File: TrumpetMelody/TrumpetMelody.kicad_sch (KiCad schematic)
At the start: 75 parts, among them J1 USB_B_Micro, J2 Conn_01x05, SW1 SW_Push, SW2 SW_SPST, SW3 SW_SPST, SW4 SW_SPST, U1 STM32F411RETx, U2 TLV62565DBVR, U3 MAX98357AETE+T, Y1 8MHz

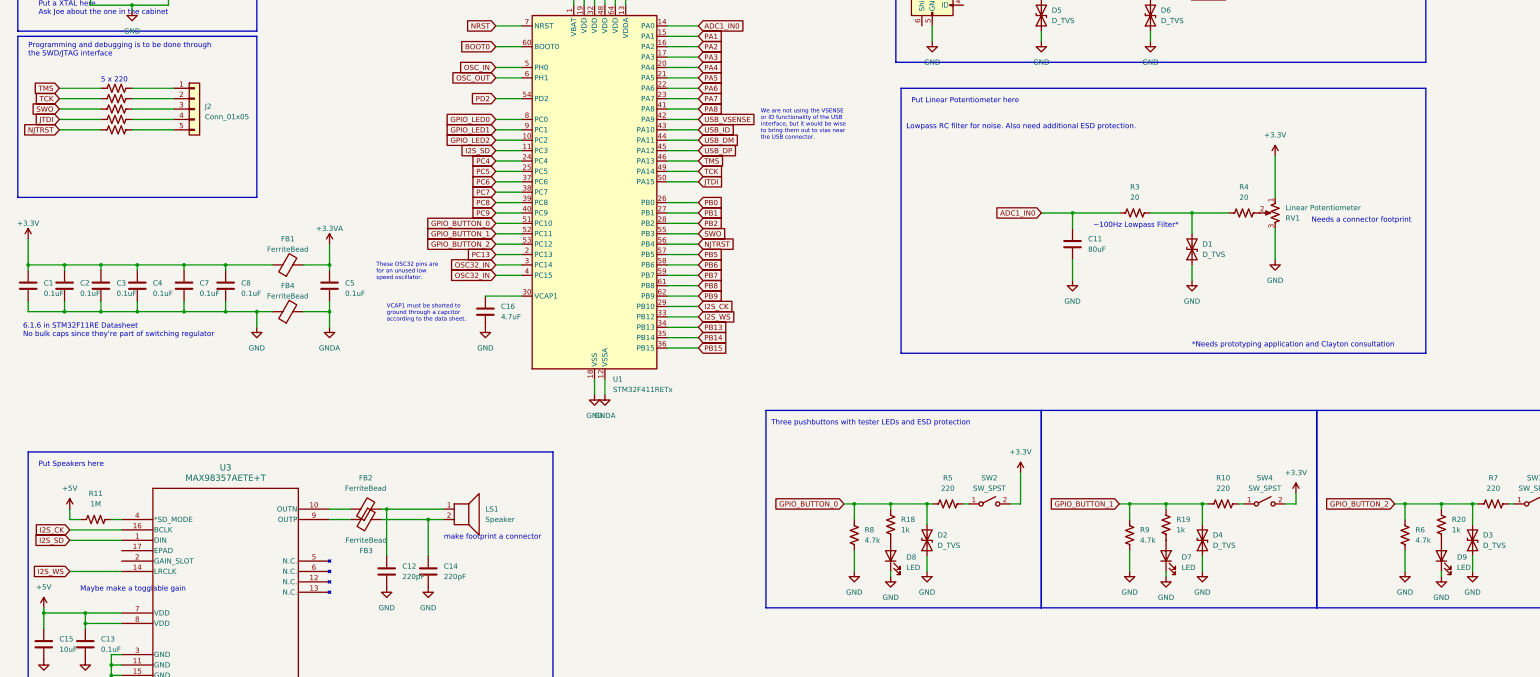
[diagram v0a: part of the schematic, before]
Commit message: Added gain resistor to speaker circuit
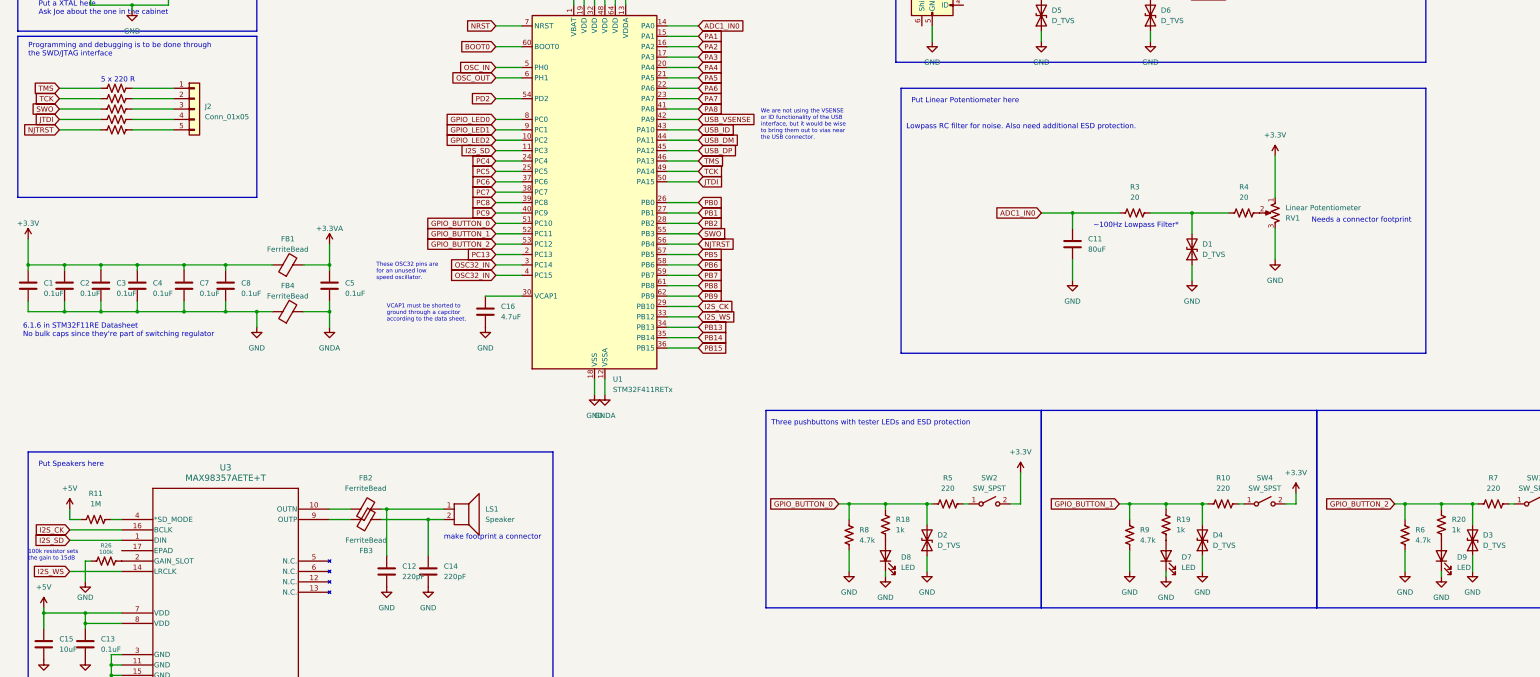
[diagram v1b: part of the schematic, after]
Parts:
- added R26: 100k, Resistor_SMD:R_0805_2012Metric_Pad1.20x1.40mm_HandSolder, symbol Device:R_US
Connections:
- net GND: now also R26.1
- net at U3.2 (GAIN_SLOT): now also R26.2
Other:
- note added: "100k resistor sets the gain to 15dB"
- note added: "5 x 220 R"
- note removed: "*Needs prototyping application and Clayton consultation"
- note removed: "5 x 220"
- note removed: "Maybe make a togglable gain"
- moved on the sheet: D8, R18, R8
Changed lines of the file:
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@@
   (junction (at 26.67 175.26) (diameter 0) (color 0 0 0 0)
   )
-  (junction (at 228.6 222.25) (diameter 0) (color 0 0 0 0)
+  (junction (at 227.33 222.25) (diameter 0) (color 0 0 0 0)
   )
   (junction (at 370.84 222.25) (diameter 0) (color 0 0 0 0)
@@
   (junction (at 31.75 248.92) (diameter 0) (color 0 0 0 0)
   )
-  (junction (at 219.71 222.25) (diameter 0) (color 0 0 0 0)
+  (junction (at 218.44 222.25) (diameter 0) (color 0 0 0 0)
   )
   (junction (at 354.33 222.25) (diameter 0) (color 0 0 0 0)
@@
     (stroke (width 0) (type default))
   )
-  (wire (pts (xy 228.6 222.25) (xy 228.6 223.52))
+  (wire (pts (xy 227.33 222.25) (xy 227.33 223.52))
     (stroke (width 0) (type default))
   )
@@
     (stroke (width 0) (type default))
   )
-  (wire (pts (xy 219.71 222.25) (xy 228.6 222.25))
+  (wire (pts (xy 218.44 222.25) (xy 227.33 222.25))
     (stroke (width 0) (type default))
   )
@@
     (stroke (width 0) (type default))
   )
-  (wire (pts (xy 228.6 238.76) (xy 228.6 240.03))
+  (wire (pts (xy 227.33 238.76) (xy 227.33 240.03))
     (stroke (width 0) (type default))
   )
@@
     (stroke (width 0) (type default))
   )
+  (wire (pts (xy 31.75 236.22) (xy 31.75 241.3))
+    (stroke (width 0) (type default))
+  )
   (wire (pts (xy 273.05 154.94) (xy 273.05 151.13))
     (stroke (width 0) (type default))
@@
     (stroke (width 0) (type default))
   )
+  (wire (pts (xy 33.02 236.22) (xy 31.75 236.22))
+    (stroke (width 0) (type default))
+  )
   (wire (pts (xy 17.78 157.48) (xy 17.78 163.83))
     (stroke (width 0) (type default))
@@
     (stroke (width 0) (type default))
   )
-  (wire (pts (xy 217.17 222.25) (xy 219.71 222.25))
+  (wire (pts (xy 215.9 222.25) (xy 218.44 222.25))
     (stroke (width 0) (type default))
   )
@@
     (stroke (width 0) (type default))
   )
-  (wire (pts (xy 219.71 233.68) (xy 219.71 238.76))
+  (wire (pts (xy 218.44 233.68) (xy 218.44 238.76))
     (stroke (width 0) (type default))
   )
@@
     (stroke (width 0) (type default))
   )
-  (wire (pts (xy 219.71 222.25) (xy 219.71 226.06))
+  (wire (pts (xy 218.44 222.25) (xy 218.44 226.06))
     (stroke (width 0) (type default))
   )
@@
     (stroke (width 0) (type default))
   )
-  (wire (pts (xy 228.6 222.25) (xy 237.49 222.25))
+  (wire (pts (xy 227.33 222.25) (xy 237.49 222.25))
     (stroke (width 0) (type default))
   )
@@
     (effects (font (size 1.27 1.27)) (justify left bottom))
   )
-  (text "5 x 220" (at 35.56 119.38 0)
+  (text "5 x 220 R" (at 35.56 119.38 0)
     (effects (font (size 1.27 1.27)) (justify left bottom))
   )
@@
     (effects (font (size 1.27 1.27)) (justify left bottom))
   )
+  (text "100k resistor sets \nthe gain to 15dB" (at 17.78 236.22 0)
+    (effects (font (size 1 1)) (justify left bottom))
+  )
   (text "6.1.6 in STM32F11RE Datasheet\nNo bulk caps since they're part of switching regulator"
     (at 16.51 181.61 0)
@@
     (effects (font (size 1.27 1.27)) (justify left bottom))
   )
-  (text "*Needs prototyping application and Clayton consultation"
-    (at 302.26 184.15 0)
-    (effects (font (size 1.27 1.27)) (justify left bottom))
-  )
-  (text "Maybe make a togglable gain" (at 30.48 243.84 0)
-    (effects (font (size 1.27 1.27)) (justify left bottom))
-  )
   (global_label "SWO" (shape input) (at 181.61 156.21 0) (fields_autoplaced)
     (effects (font (size 1.27 1.27)) (justify left))
@@
     )
   )
-  (global_label "GPIO_BUTTON_0" (shape input) (at 217.17 222.25 180) (fields_autoplaced)
+  (global_label "GPIO_BUTTON_0" (shape input) (at 215.9 222.25 180) (fields_autoplaced)
     (effects (font (size 1.27 1.27)) (justify right))
-    (property "Intersheetrefs" "${INTERSHEET_REFS}" (at 199.3681 222.25 0)
+    (property "Intersheetrefs" "${INTERSHEET_REFS}" (at 198.0981 222.25 0)
       (effects (font (size 1.27 1.27)) (justify right) hide)
     )
@@
     )
   )
-  (symbol (lib_id "power:GND") (at 228.6 240.03 0) (unit 1)
+  (symbol (lib_id "power:GND") (at 227.33 240.03 0) (unit 1)
     (in_bom yes) (on_board yes) (dnp no) (fields_autoplaced)
-    (property "Reference" "#PWR045" (at 228.6 246.38 0)
+    (property "Reference" "#PWR045" (at 227.33 246.38 0)
       (effects (font (size 1.27 1.27)) hide)
     )
-    (property "Value" "GND" (at 228.6 245.11 0)
+    (property "Value" "GND" (at 227.33 245.11 0)
       (effects (font (size 1.27 1.27)))
     )
-    (property "Footprint" "" (at 228.6 240.03 0)
+    (property "Footprint" "" (at 227.33 240.03 0)
       (effects (font (size 1.27 1.27)) hide)
     )
-    (property "Datasheet" "" (at 228.6 240.03 0)
+    (property "Datasheet" "" (at 227.33 240.03 0)
       (effects (font (size 1.27 1.27)) hide)
     )
@@
     )
   )
-  (symbol (lib_id "Device:LED") (at 228.6 234.95 90) (unit 1)
+  (symbol (lib_id "Device:LED") (at 227.33 234.95 90) (unit 1)
     (in_bom yes) (on_board yes) (dnp no) (fields_autoplaced)
-    (property "Reference" "D8" (at 232.41 235.2675 90)
+    (property "Reference" "D8" (at 231.14 235.2675 90)
       (effects (font (size 1.27 1.27)) (justify right))
     )
-    (property "Value" "LED" (at 232.41 237.8075 90)
+    (property "Value" "LED" (at 231.14 237.8075 90)
       (effects (font (size 1.27 1.27)) (justify right))
     )
-    (property "Footprint" "" (at 228.6 234.95 0)
+    (property "Footprint" "" (at 227.33 234.95 0)
       (effects (font (size 1.27 1.27)) hide)
     )
-    (property "Datasheet" "~" (at 228.6 234.95 0)
+    (property "Datasheet" "~" (at 227.33 234.95 0)
       (effects (font (size 1.27 1.27)) hide)
     )
@@
     )
   )
-  (symbol (lib_id "Device:R_US") (at 219.71 229.87 180) (unit 1)
+  (symbol (lib_id "Device:R_US") (at 218.44 229.87 180) (unit 1)
     (in_bom yes) (on_board yes) (dnp no) (fields_autoplaced)
-    (property "Reference" "R8" (at 222.25 228.6 0)
+    (property "Reference" "R8" (at 220.98 228.6 0)
       (effects (font (size 1.27 1.27)) (justify right))
     )
-    (property "Value" "4.7k" (at 222.25 231.14 0)
+    (property "Value" "4.7k" (at 220.98 231.14 0)
       (effects (font (size 1.27 1.27)) (justify right))
     )
-    (property "Footprint" "" (at 218.694 229.616 90)
+    (property "Footprint" "" (at 217.424 229.616 90)
       (effects (font (size 1.27 1.27)) hide)
     )
-    (property "Datasheet" "~" (at 219.71 229.87 0)
+    (property "Datasheet" "~" (at 218.44 229.87 0)
       (effects (font (size 1.27 1.27)) hide)
     )
@@
     )
   )
-  (symbol (lib_id "Device:R_US") (at 228.6 227.33 180) (unit 1)
+  (symbol (lib_id "Device:R_US") (at 227.33 227.33 180) (unit 1)
     (in_bom yes) (on_board yes) (dnp no) (fields_autoplaced)
-    (property "Reference" "R18" (at 231.14 226.06 0)
+    (property "Reference" "R18" (at 229.87 226.06 0)
       (effects (font (size 1.27 1.27)) (justify right))
     )
-    (property "Value" "1k" (at 231.14 228.6 0)
+    (property "Value" "1k" (at 229.87 228.6 0)
       (effects (font (size 1.27 1.27)) (justify right))
     )
-    (property "Footprint" "Resistor_SMD:R_0805_2012Metric_Pad1.20x1.40mm_HandSolder" (at 227.584 227.076 90)
+    (property "Footprint" "Resistor_SMD:R_0805_2012Metric_Pad1.20x1.40mm_HandSolder" (at 226.314 227.076 90)
       (effects (font (size 1.27 1.27)) hide)
     )
-    (property "Datasheet" "~" (at 228.6 227.33 0)
+    (property "Datasheet" "~" (at 227.33 227.33 0)
       (effects (font (size 1.27 1.27)) hide)
     )
@@
     )
   )
+  (symbol (lib_id "power:GND") (at 31.75 241.3 0) (unit 1)
+    (in_bom yes) (on_board yes) (dnp no)
+    (property "Reference" "#PWR049" (at 31.75 247.65 0)
+      (effects (font (size 1.27 1.27)) hide)
+    )
+    (property "Value" "GND" (at 31.75 245.11 0)
+      (effects (font (size 1.27 1.27)))
+    )
+    (property "Footprint" "" (at 31.75 241.3 0)
+      (effects (font (size 1.27 1.27)) hide)
+    )
+    (property "Datasheet" "" (at 31.75 241.3 0)
+      (effects (font (size 1.27 1.27)) hide)
+    )
+    (pin "1")
+    (instances
+      (project "TrumpetMelody"
+        (path "/646bb87a-580f-408c-a344-dec391089cbb"
+          (reference "#PWR049") (unit 1)
+        )
+      )
+    )
+  )
   (symbol (lib_id "TrumpetMelody_Symbol_Library:MAX98357AETE+T") (at 40.64 226.06 0) (unit 1)
     (in_bom yes) (on_board yes) (dnp no) (fields_autoplaced)
@@
     )
   )
-  (symbol (lib_id "power:GND") (at 219.71 238.76 0) (unit 1)
+  (symbol (lib_id "power:GND") (at 218.44 238.76 0) (unit 1)
     (in_bom yes) (on_board yes) (dnp no) (fields_autoplaced)
-    (property "Reference" "#PWR025" (at 219.71 245.11 0)
+    (property "Reference" "#PWR025" (at 218.44 245.11 0)
       (effects (font (size 1.27 1.27)) hide)
     )
-    (property "Value" "GND" (at 219.71 243.84 0)
+    (property "Value" "GND" (at 218.44 243.84 0)
       (effects (font (size 1.27 1.27)))
     )
-    (property "Footprint" "" (at 219.71 238.76 0)
+    (property "Footprint" "" (at 218.44 238.76 0)
       (effects (font (size 1.27 1.27)) hide)
     )
-    (property "Datasheet" "" (at 219.71 238.76 0)
+    (property "Datasheet" "" (at 218.44 238.76 0)
       (effects (font (size 1.27 1.27)) hide)
     )
@@
         )
       )
+    )
+  )
+  (symbol (lib_id "Device:R_US") (at 36.83 236.22 90) (unit 1)
+    (in_bom yes) (on_board yes) (dnp no)
+    (property "Reference" "R26" (at 36.83 232.41 90)
+      (effects (font (size 1 1)))
+    )
+    (property "Value" "100k" (at 36.83 234 90)
+      (effects (font (size 1 1)))
+    )
+    (property "Footprint" "Resistor_SMD:R_0805_2012Metric_Pad1.20x1.40mm_HandSolder" (at 37.084 235.204 90)
+      (effects (font (size 1.27 1.27)) hide)
+    )
+    (property "Datasheet" "~" (at 36.83 236.22 0)
+      (effects (font (size 1.27 1.27)) hide)
+    )
+    (pin "1")
+    (pin "2")
+    (instances
+      (project "TrumpetMelody"
+        (path "/646bb87a-580f-408c-a344-dec391089cbb"
+          (reference "R26") (unit 1)
+        )
+      )

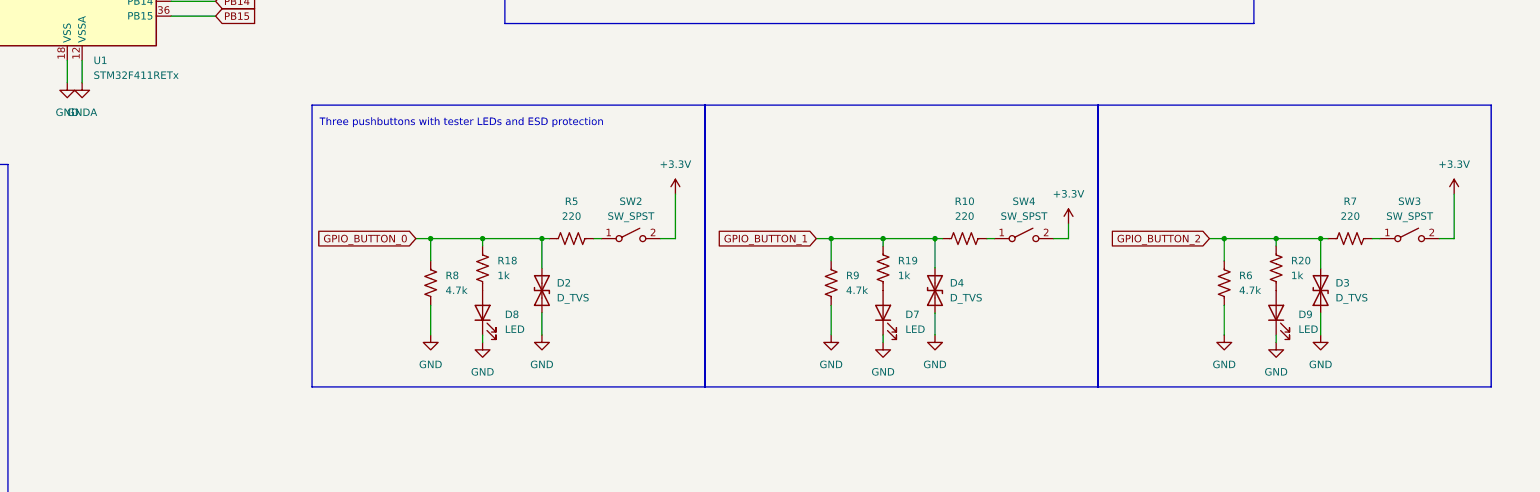
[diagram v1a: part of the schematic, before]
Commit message: Added debouncing caps to the buttons
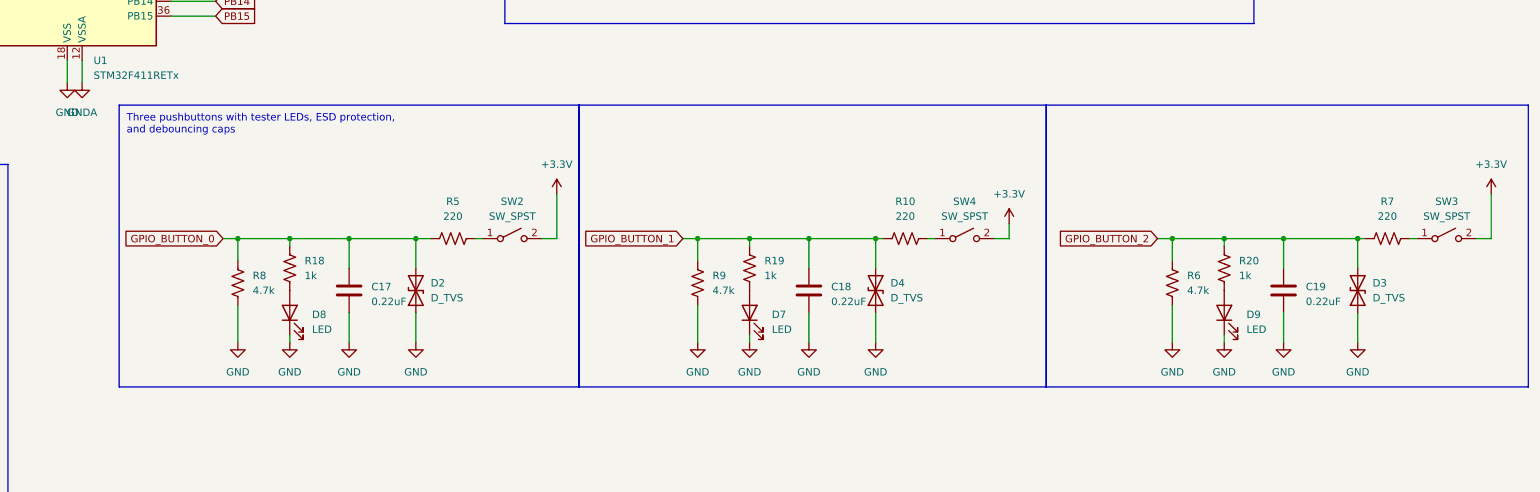
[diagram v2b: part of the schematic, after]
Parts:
- added C17, C18, C19: 0.22uF, Capacitor_SMD:C_0805_2012Metric_Pad1.18x1.45mm_HandSolder, symbol Device:C
- D7, D8, D9: footprint (none) -> LED_SMD:LED_0805_2012Metric_Pad1.15x1.40mm_HandSolder
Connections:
- net GND: now also C17.2, C18.2, C19.2
- net GPIO_BUTTON_0: now also C17.1
- net GPIO_BUTTON_1: now also C18.1
- net GPIO_BUTTON_2: now also C19.1
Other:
- note added: "Three pushbuttons with tester LEDs, ESD protection, and debouncing caps"
- note removed: "Three pushbuttons with tester LEDs and ESD protection"
- moved on the sheet: D2, D3, D4, D7, D8, D9, R10, R18, R19, R20, R5, R6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

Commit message: test
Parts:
- removed C10: ~10pF, symbol Device:C
- removed Y1: 8MHz, symbol Device:Crystal
- added U4: MAX7375AXR805, Package_TO_SOT_SMD:SOT-323_SC-70, symbol Oscillator:MAX7375AXR805
- C9: value ~10pF -> 0.1uF; footprint (none) -> Capacitor_SMD:C_0805_2012Metric_Pad1.18x1.45mm_HandSolder
- J2: footprint (none) -> Connector_PinHeader_2.54mm:PinHeader_1x05_P2.54mm_Vertical
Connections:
- net +3.3V: now also C9.1, U4.1 (V+)
- net GND: now also U4.3 (GND)
- net OSC_IN: now also U4.2 (CLOCK); no longer C9.1
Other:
- note added: "OSC_OUT is left open when using a silicon oscillator"
- note added: "The datasheet says that you can use the microcontrollers decoupling capacitors by mounting the oscillator as close to them as possible, instead of using a separate capacitor."
- note removed: "Put a XTAL here Ask Joe about the one in the cabinet"
- note removed: "We need to pick an oscillator soon Carson has some notes on that and picking the caps STM32F411RE Datasheet pg 85 AN2867 pg 13 and the whole thing really"

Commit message: finished schematic and intialized PCB
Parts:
- removed C15: 10uF, symbol Device:C
- removed SW2, SW3, SW4: SW_SPST, symbol Switch:SW_SPST
- removed U3: MAX98357AETE+T, 21-0136I_T1633-4_MXM, symbol TrumpetMelody_Symbol_Library:MAX98357AETE+T
- added C10: 10uF, Capacitor_SMD:C_0805_2012Metric_Pad1.18x1.45mm_HandSolder, symbol Device:C
- added H1, H2, H3, H4: MountingHole, MountingHole:MountingHole_3.5mm, symbol Mechanical:MountingHole
- added J3, J4: 640456-3, TrumpetMelodyFootprintLibrary:TE_640456-3, symbol TrumpetMelody_Symbol_Library:640456-3
- added U3: MAX98357AETE_T, TrumpetMelodyFootprintLibrary:QFN50P300X300X80-17N, symbol TrumpetMelody_Symbol_Library:MAX98357AETE_T
- C1, C12, C13, C14, C2, C3, C4, C5, C6, C7, C8: footprint (none) -> Capacitor_SMD:C_0805_2012Metric_Pad1.18x1.45mm_HandSolder
- C11: value 80uF -> 10uF; footprint (none) -> Capacitor_SMD:C_0805_2012Metric_Pad1.18x1.45mm_HandSolder
- D1, D2, D3, D4, D5, D6: footprint (none) -> Diode_SMD:D_01005_0402Metric_Pad0.57x0.30mm_HandSolder
- D10: footprint (none) -> LED_SMD:LED_0805_2012Metric_Pad1.15x1.40mm_HandSolder
- FB1, FB2, FB3, FB4: footprint (none) -> TrumpetMelodyFootprintLibrary:FB_LI0805G201R-10
- J1: footprint (none) -> TrumpetMelodyFootprintLibrary:TE_2172034-1
- LS1, RV1: footprint (none) -> TrumpetMelodyFootprintLibrary:TE_640456-3
- R1, R10, R11, R12, R13, R2, R21, R22, R23, R24, R25, R4, R5, R6, R7, R8, R9: footprint (none) -> Resistor_SMD:R_0805_2012Metric_Pad1.20x1.40mm_HandSolder
- R3: value 20 -> 150; footprint (none) -> Resistor_SMD:R_0805_2012Metric_Pad1.20x1.40mm_HandSolder
- SW1: footprint (none) -> Button_Switch_SMD:SW_SPST_PTS645
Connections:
- net +3.3V: now also J4.1, J4.2, J4.3
- net +5V: now also C10.1, U3.7 (VDD), U3.8 (VDD__1)
- net GND: now also C10.2, U3.11 (GND__1), U3.15 (GND__2), U3.3 (GND)
- net I2S_CK: now also U3.16 (BCLK)
- net I2S_SD: now also U3.1 (DIN)
- net I2S_WS: now also U3.14 (LRCLK)
- net USB_ID_Connector: now reaches J1.4 (ID)
- net USB_Shield: now reaches J1.6 (Shield)
- net BUTTON_1: now reaches R10.2
- net BUTTON_1: now also J3.2
- net BUTTON_2: now reaches R7.2
- net BUTTON_2: now also J3.3
- net BUTTON_0: now reaches R5.2
- net BUTTON_0: now also J3.1
- net at FB3.2: now also U3.9 (OUTP)
- net at R11.2: now also U3.4 (SD_MODE)
- net at FB2.1: now also U3.10 (OUTN)
- net at R26.2: now also U3.2 (GAIN_SLOT)
- new net PadMax: U3.17 (EP)
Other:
- note added: "Single Pull-Single Throw switches here"
- moved on the sheet: C12, C14, FB2, FB3, LS1, R11, R26
